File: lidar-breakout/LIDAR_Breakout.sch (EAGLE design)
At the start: 85 parts, among them P1 0436500200, X1 XTAL-3.2X2.5

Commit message: Aligned schematic on grid, cleaned up routing, switched power symbol
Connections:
- net VCC1 renamed VCC_1
- net VCC2 renamed VCC_2
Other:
- moved on the sheet: C1, C10, C11, C12, C13, C14, C15, C16, C17, C18, C19, C21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

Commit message: redrawn logic blocks
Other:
- note added: "Arduino"
- note added: "Lidar headers"
- note added: "Status Led"
- moved on the sheet: C21, C23, C3, C4, D1, ETH1, PB1, PB2, R1, R15, R16, R4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

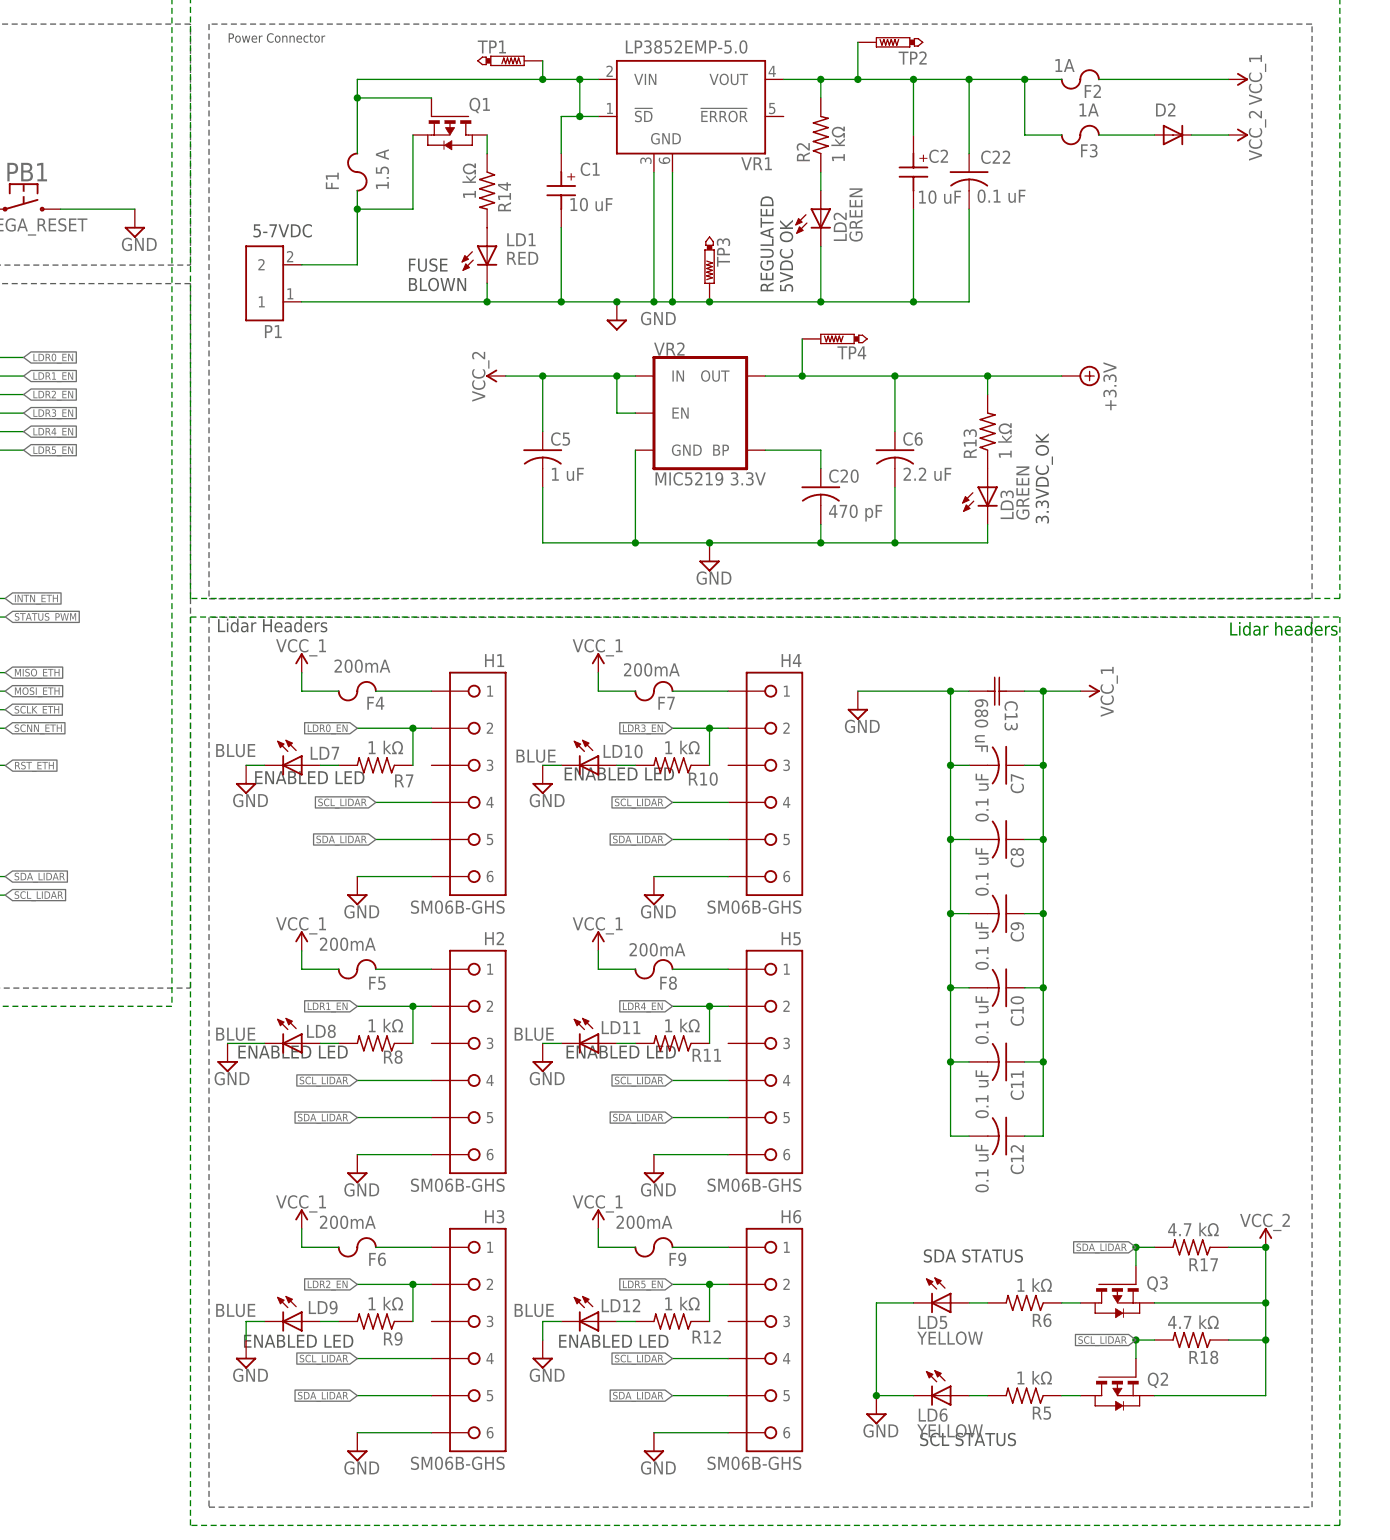
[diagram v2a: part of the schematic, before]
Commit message: removed individual LIDAR fuses and added power header
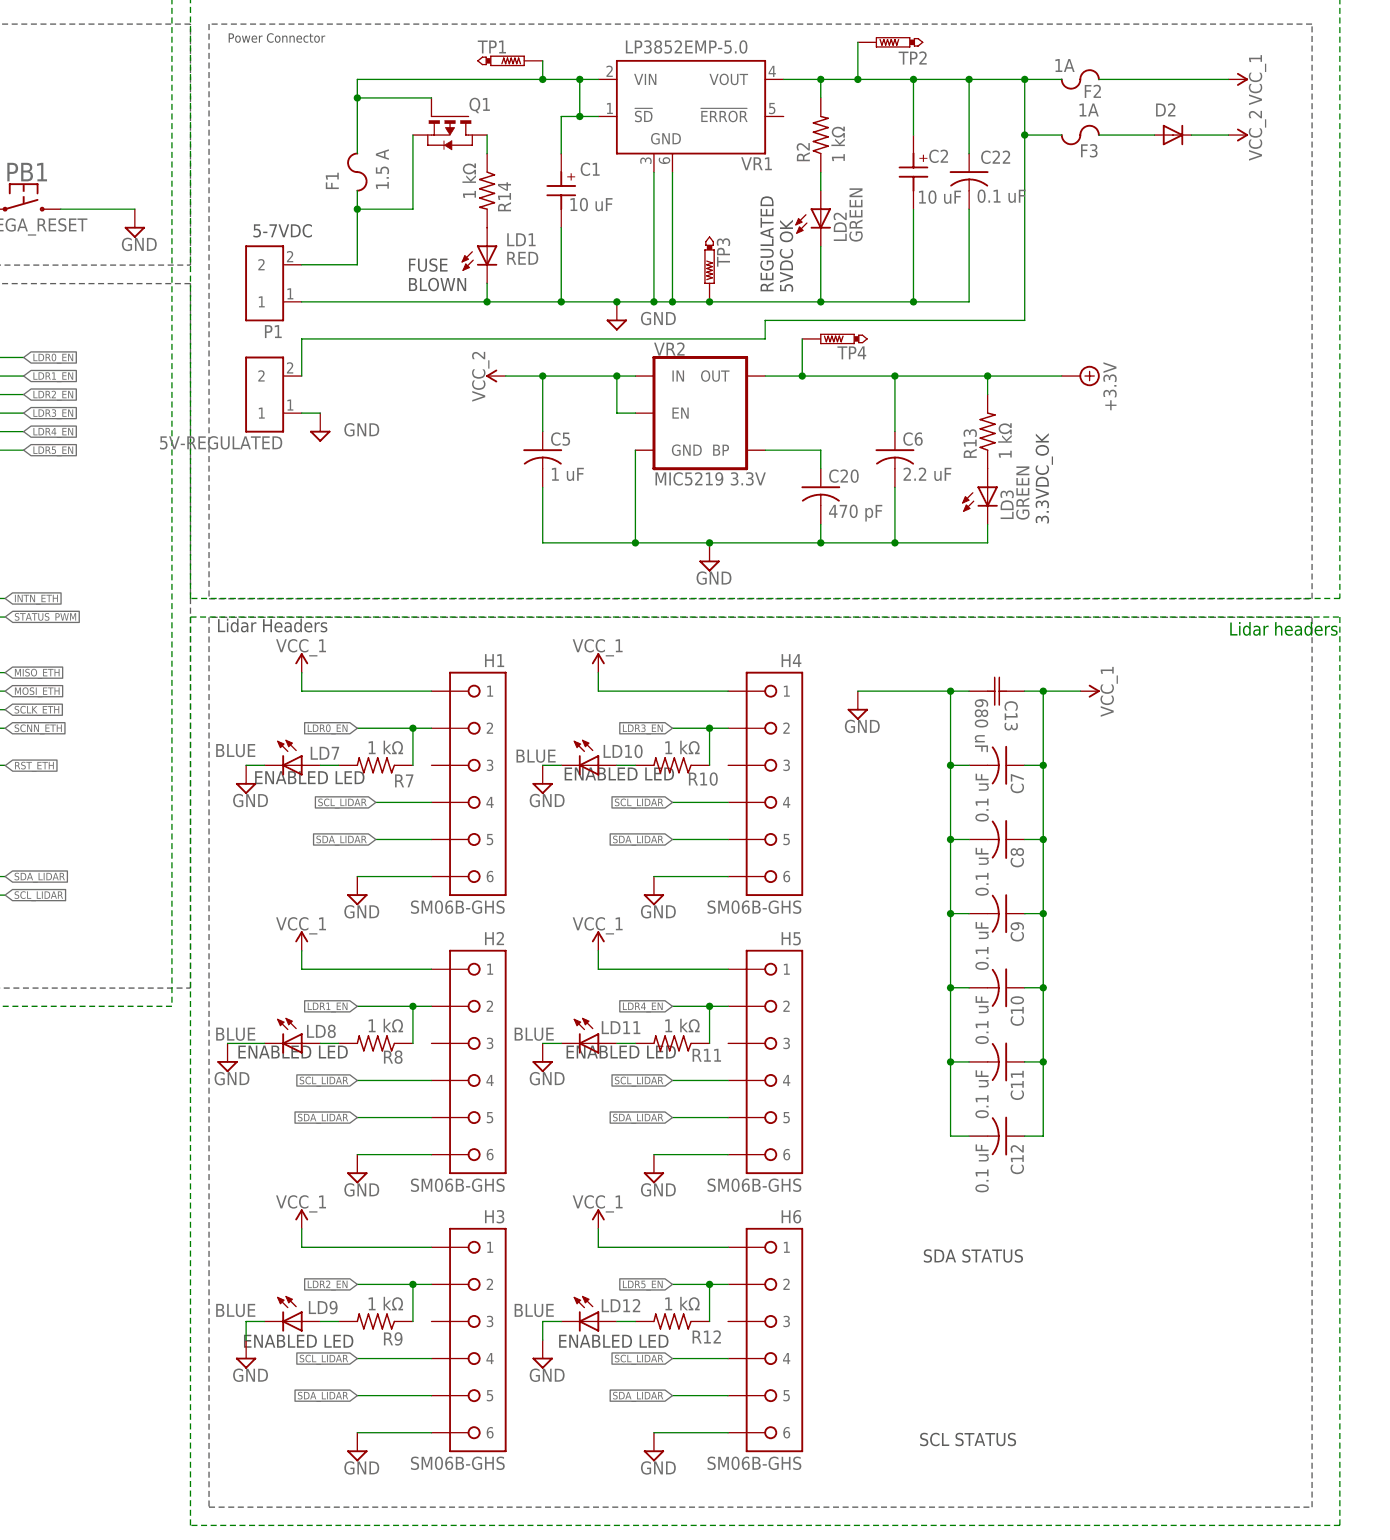
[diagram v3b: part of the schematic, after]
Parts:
- removed F4, F5, F6, F7, F8, F9: 200mA, RoboJackets-Fuses:CHIP_FUSE0603
- removed LD5, LD6: YELLOW, led:LEDCHIP-LED0603
- removed Q2, Q3: (no value), RoboJackets-Discrete:PMOS
- removed R17, R18: 4.7 kΩ, rcl:R-US_R0603
- removed R5, R6: 1 kΩ, rcl:R-US_R0603
- added 5V-REGULATED: 0436500200, 0436500200:0436500200
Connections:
- removed net N$10: Q3.D, R6.1
- removed net N$8: Q2.D, R5.1
- removed net SCL_STS_LED: LD6.A, R5.2
- removed net SDA_STS_LED: LD5.A, R6.2
- removed net VCC_LDR0: F4.1, H1.1
- removed net VCC_LDR1: F5.1, H2.1
- removed net VCC_LDR2: F6.1, H3.1
- removed net VCC_LDR3: F7.1, H4.1
- removed net VCC_LDR4: F8.1, H5.1
- removed net VCC_LDR5: F9.1, H6.1
- net GND: now also 5V-REGULATED.1; no longer LD5.C, LD6.C
- net SCL_LIDAR: no longer Q2.G, R18.2
- net SDA_LIDAR: no longer Q3.G, R17.2
- net VCC_1: now also H1.1, H2.1, H3.1, H4.1, H5.1, H6.1; no longer F4.2, F5.2, F6.2, F7.2, F8.2, F9.2
- net VCC_2: no longer Q2.S, Q3.S, R17.1, R18.1
- net VOUT: now also 5V-REGULATED.2

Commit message: added i2c activity led, added reverse polarity protection, changed layer to info, labeled crystal
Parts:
- added D3: (no value), RoboJackets-Diodes:DIODE-DO-214AC
- added I2C_ACT: BLUE, led:LEDCHIP-LED0603
- added Q2: (no value), RoboJackets-Discrete:PMOS
- added R3: 1 kΩ, rcl:R-US_R0603
- X1: value XTAL-3.2X2.5 -> 16MHz
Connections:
- new net I2C_ACTIVITY: MC1.PB5(OC1A/ADC12/!OC4B), R3.1
- new net N$2: D3.A, P1.2
- new net N$8: I2C_ACT.A, R3.2
- new net N$9: 5V-REGULATED.2, Q2.D
- net GND: now also I2C_ACT.C, Q2.G
- net UVCC: now also D3.C; no longer P1.2
- net VOUT: now also Q2.S; no longer 5V-REGULATED.2
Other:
- note added: "I2C Activity Led"
- note removed: "Lidar headers"
- note removed: "Microcontroller"
- note removed: "Reset PB"
- note removed: "SCL STATUS"
- note removed: "SDA STATUS"
- note removed: "Status NeoPixel"
- moved on the sheet: 5V-REGULATED, P1
